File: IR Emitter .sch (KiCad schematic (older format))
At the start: 26 parts, among them U11 ULN2003APWR, U12 SMT_0540-S-R

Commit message: removed SD Card
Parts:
- R30, R31, R32, R33, R34, R35, R36: renamed from R?; footprint (none) -> Resistors_SMD:R_0603
- U11: footprint sop:TSSOP16 -> micromouse:ULN2003APWR
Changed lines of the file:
@@
 F 0 "U11" H 1850 4925 60  0000 L CNN
 F 1 "ULN2003APWR" H 1850 4825 60  0000 L CNN
-F 2 "sop:TSSOP16" H 1650 4675 60  0001 C CNN
+F 2 "micromouse:ULN2003APWR" H 1650 4675 60  0001 C CNN
 F 3 "" H 1650 4675 60  0001 C CNN
 	1    1650 4675
@@
 IR Emitter
 $Comp
-L R R?
+L R R30
 U 1 1 5976EE2D
 P 1300 4675
-F 0 "R?" V 1380 4675 50  0000 C CNN
+F 0 "R30" V 1380 4675 50  0000 C CNN
 F 1 "0" V 1300 4675 50  0000 C CNN
-F 2 "" V 1230 4675 50  0001 C CNN
+F 2 "Resistors_SMD:R_0603" V 1230 4675 50  0001 C CNN
 F 3 "" H 1300 4675 50  0001 C CNN
 	1    1300 4675
@@
 $EndComp
 $Comp
-L R R?
+L R R32
 U 1 1 5976F354
 P 1300 4875
-F 0 "R?" V 1380 4875 50  0000 C CNN
+F 0 "R32" V 1380 4875 50  0000 C CNN
 F 1 "0" V 1300 4875 50  0000 C CNN
-F 2 "" V 1230 4875 50  0001 C CNN
+F 2 "Resistors_SMD:R_0603" V 1230 4875 50  0001 C CNN
 F 3 "" H 1300 4875 50  0001 C CNN
 	1    1300 4875
@@
 $EndComp
 $Comp
-L R R?
+L R R31
 U 1 1 5976F3DE
 P 1300 4775
-F 0 "R?" V 1380 4775 50  0000 C CNN
+F 0 "R31" V 1380 4775 50  0000 C CNN
 F 1 "0" V 1300 4775 50  0000 C CNN
-F 2 "" V 1230 4775 50  0001 C CNN
+F 2 "Resistors_SMD:R_0603" V 1230 4775 50  0001 C CNN
 F 3 "" H 1300 4775 50  0001 C CNN
 	1    1300 4775
@@
 $EndComp
 $Comp
-L R R?
+L R R33
 U 1 1 5976F49C
 P 1300 4975
-F 0 "R?" V 1380 4975 50  0000 C CNN
+F 0 "R33" V 1380 4975 50  0000 C CNN
 F 1 "0" V 1300 4975 50  0000 C CNN
-F 2 "" V 1230 4975 50  0001 C CNN
+F 2 "Resistors_SMD:R_0603" V 1230 4975 50  0001 C CNN
 F 3 "" H 1300 4975 50  0001 C CNN
 	1    1300 4975
@@
 $EndComp
 $Comp
-L R R?
+L R R34
 U 1 1 5976F4F7
 P 1300 5075
-F 0 "R?" V 1380 5075 50  0000 C CNN
+F 0 "R34" V 1380 5075 50  0000 C CNN
 F 1 "0" V 1300 5075 50  0000 C CNN
-F 2 "" V 1230 5075 50  0001 C CNN
+F 2 "Resistors_SMD:R_0603" V 1230 5075 50  0001 C CNN
 F 3 "" H 1300 5075 50  0001 C CNN
 	1    1300 5075
@@
 $EndComp
 $Comp
-L R R?
+L R R35
 U 1 1 5976F557
 P 1300 5175
-F 0 "R?" V 1380 5175 50  0000 C CNN
+F 0 "R35" V 1380 5175 50  0000 C CNN
 F 1 "0" V 1300 5175 50  0000 C CNN
-F 2 "" V 1230 5175 50  0001 C CNN
+F 2 "Resistors_SMD:R_0603" V 1230 5175 50  0001 C CNN
 F 3 "" H 1300 5175 50  0001 C CNN
 	1    1300 5175
@@
 $EndComp
 $Comp
-L R R?
+L R R36
 U 1 1 5976F840
 P 1300 5275
-F 0 "R?" V 1380 5275 50  0000 C CNN
+F 0 "R36" V 1380 5275 50  0000 C CNN
 F 1 "0" V 1300 5275 50  0000 C CNN
-F 2 "" V 1230 5275 50  0001 C CNN
+F 2 "Resistors_SMD:R_0603" V 1230 5275 50  0001 C CNN
 F 3 "" H 1300 5275 50  0001 C CNN
 	1    1300 5275

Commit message: Added MPU-6500
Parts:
- removed R30, R31, R32, R33, R34, R35, R36: 0, Resistors_SMD:R_0603, symbol R
- added C30, C31: C, Capacitors_SMD:C_0603, symbol C
- D10, D12, D13, D8, D9: footprint LEDs:LED_D5.0mm_Horizontal_O3.81mm_Z3.0mm -> micromouse:IR-Emitter
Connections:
- wire segments 55 -> 53
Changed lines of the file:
@@
 EESchema Schematic File Version 2
+LIBS:device
+LIBS:Micromouse
 LIBS:power
-LIBS:device
 LIBS:transistors
 LIBS:conn
@@
 LIBS:contrib
 LIBS:valves
-LIBS:Micromouse
 LIBS:1_PJC-Sandbox
 LIBS:Micromouse1.2-cache
@@
 $Descr A4 11693 8268
 encoding utf-8
-Sheet 4 7
+Sheet 4 8
 Title ""
 Date ""
@@
 F 0 "D9" H 3495 3520 50  0000 L CNN
 F 1 "IRL81A" H 3435 3340 50  0000 C CNN
-F 2 "LEDs:LED_D5.0mm_Horizontal_O3.81mm_Z3.0mm" H 3475 3625 50  0001 C CNN
+F 2 "micromouse:IR-Emitter" H 3475 3625 50  0001 C CNN
 F 3 "" H 3425 3450 50  0000 C CNN
 	1    3475 3450
@@
 F 0 "D10" H 5020 3495 50  0000 L CNN
 F 1 "IRL81A" H 4960 3315 50  0000 C CNN
-F 2 "LEDs:LED_D5.0mm_Horizontal_O3.81mm_Z3.0mm" H 5000 3600 50  0001 C CNN
+F 2 "micromouse:IR-Emitter" H 5000 3600 50  0001 C CNN
 F 3 "" H 4950 3425 50  0000 C CNN
 	1    5000 3425
@@
 F 0 "D12" H 7220 3495 50  0000 L CNN
 F 1 "IRL81A" H 7160 3315 50  0000 C CNN
-F 2 "LEDs:LED_D5.0mm_Horizontal_O3.81mm_Z3.0mm" H 7200 3600 50  0001 C CNN
+F 2 "micromouse:IR-Emitter" H 7200 3600 50  0001 C CNN
 F 3 "" H 7150 3425 50  0000 C CNN
 	1    7200 3425
@@
 F 0 "D8" H 2995 3520 50  0000 L CNN
 F 1 "IRL81A" H 2935 3340 50  0000 C CNN
-F 2 "LEDs:LED_D5.0mm_Horizontal_O3.81mm_Z3.0mm" H 2975 3625 50  0001 C CNN
+F 2 "micromouse:IR-Emitter" H 2975 3625 50  0001 C CNN
 F 3 "" H 2925 3450 50  0000 C CNN
 	1    2975 3450
@@
 F 0 "D13" H 7720 3495 50  0000 L CNN
 F 1 "IRL81A" H 7660 3315 50  0000 C CNN
-F 2 "LEDs:LED_D5.0mm_Horizontal_O3.81mm_Z3.0mm" H 7700 3600 50  0001 C CNN
+F 2 "micromouse:IR-Emitter" H 7700 3600 50  0001 C CNN
 F 3 "" H 7650 3425 50  0000 C CNN
 	1    7700 3425
@@
 	2975 3350 2975 2925
 Wire Wire Line
-	2650 2925 7700 2925
+	2650 2925 8200 2925
 Wire Wire Line
 	7700 2925 7700 3325
@@
 Text Notes 3900 1400 0    394  ~ 79
 IR Emitter
-$Comp
-L R R30
-U 1 1 5976EE2D
-P 1300 4675
-F 0 "R30" V 1380 4675 50  0000 C CNN
-F 1 "0" V 1300 4675 50  0000 C CNN
-F 2 "Resistors_SMD:R_0603" V 1230 4675 50  0001 C CNN
-F 3 "" H 1300 4675 50  0001 C CNN
-	1    1300 4675
-	0    1    1    0
-$EndComp
-$Comp
-L R R32
-U 1 1 5976F354
-P 1300 4875
-F 0 "R32" V 1380 4875 50  0000 C CNN
-F 1 "0" V 1300 4875 50  0000 C CNN
-F 2 "Resistors_SMD:R_0603" V 1230 4875 50  0001 C CNN
-F 3 "" H 1300 4875 50  0001 C CNN
-	1    1300 4875
-	0    1    1    0
-$EndComp
-$Comp
-L R R31
-U 1 1 5976F3DE
-P 1300 4775
-F 0 "R31" V 1380 4775 50  0000 C CNN
-F 1 "0" V 1300 4775 50  0000 C CNN
-F 2 "Resistors_SMD:R_0603" V 1230 4775 50  0001 C CNN
-F 3 "" H 1300 4775 50  0001 C CNN
-	1    1300 4775
-	0    1    1    0
-$EndComp
-$Comp
-L R R33
-U 1 1 5976F49C
-P 1300 4975
-F 0 "R33" V 1380 4975 50  0000 C CNN
-F 1 "0" V 1300 4975 50  0000 C CNN
-F 2 "Resistors_SMD:R_0603" V 1230 4975 50  0001 C CNN
-F 3 "" H 1300 4975 50  0001 C CNN
-	1    1300 4975
-	0    1    1    0
-$EndComp
-$Comp
-L R R34
-U 1 1 5976F4F7
-P 1300 5075
-F 0 "R34" V 1380 5075 50  0000 C CNN
-F 1 "0" V 1300 5075 50  0000 C CNN
-F 2 "Resistors_SMD:R_0603" V 1230 5075 50  0001 C CNN
-F 3 "" H 1300 5075 50  0001 C CNN
-	1    1300 5075
-	0    1    1    0
-$EndComp
-$Comp
-L R R35
-U 1 1 5976F557
-P 1300 5175
-F 0 "R35" V 1380 5175 50  0000 C CNN
-F 1 "0" V 1300 5175 50  0000 C CNN
-F 2 "Resistors_SMD:R_0603" V 1230 5175 50  0001 C CNN
-F 3 "" H 1300 5175 50  0001 C CNN
-	1    1300 5175
-	0    1    1    0
-$EndComp
-$Comp
-L R R36
-U 1 1 5976F840
-P 1300 5275
-F 0 "R36" V 1380 5275 50  0000 C CNN
-F 1 "0" V 1300 5275 50  0000 C CNN
-F 2 "Resistors_SMD:R_0603" V 1230 5275 50  0001 C CNN
-F 3 "" H 1300 5275 50  0001 C CNN
-	1    1300 5275
-	0    1    1    0
-$EndComp
-Wire Wire Line
-	925  4675 1150 4675
-Wire Wire Line
-	1450 4675 1650 4675
-Wire Wire Line
-	1650 4775 1450 4775
-Wire Wire Line
-	1150 4775 925  4775
-Wire Wire Line
-	925  4875 1150 4875
-Wire Wire Line
-	1450 4875 1650 4875
-Wire Wire Line
-	1650 4975 1450 4975
-Wire Wire Line
-	1150 4975 925  4975
-Wire Wire Line
-	925  5075 1150 5075
-Wire Wire Line
-	1150 5175 925  5175
-Wire Wire Line
-	1150 5275 925  5275
-Wire Wire Line
-	1450 5275 1650 5275
-Wire Wire Line
-	1650 5175 1450 5175
-Wire Wire Line
-	1450 5075 1650 5075
+Wire Wire Line
+	925  4675 1650 4675
+Wire Wire Line
+	925  4775 1650 4775
+Wire Wire Line
+	925  4875 1650 4875
+Wire Wire Line
+	925  4975 1650 4975
+Wire Wire Line
+	925  5075 1650 5075
+Wire Wire Line
+	925  5175 1650 5175
+Wire Wire Line
+	925  5275 1650 5275
+$Comp
+L C C30
+U 1 1 5984FA65
+P 8000 3500
+F 0 "C30" H 8025 3600 50  0000 L CNN
+F 1 "C" H 8025 3400 50  0000 L CNN
+F 2 "Capacitors_SMD:C_0603" H 8038 3350 50  0001 C CNN
+F 3 "" H 8000 3500 50  0001 C CNN
+	1    8000 3500
+	1    0    0    -1
+$EndComp
+$Comp
+L C C31
+U 1 1 5984FA6B
+P 8400 3500
+F 0 "C31" H 8425 3600 50  0000 L CNN
+F 1 "C" H 8425 3400 50  0000 L CNN
+F 2 "Capacitors_SMD:C_0603" H 8438 3350 50  0001 C CNN
+F 3 "" H 8400 3500 50  0001 C CNN
+	1    8400 3500
+	1    0    0    -1
+$EndComp
+Wire Wire Line
+	8000 3350 8400 3350
+Wire Wire Line
+	8000 3650 8400 3650
+Connection ~ 8200 3650
+Wire Wire Line
+	8200 2925 8200 3350
+Connection ~ 8200 3350
+Connection ~ 7700 2925
+Wire Wire Line
+	8200 3654 8200 3950
+Wire Wire Line
+	8200 3950 8198 3950
+Connection ~ 8198 3950
 $EndSCHEMATC

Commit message: finished floor planning
-replaced the TC4427 and H brige by a single DRV8833 chip
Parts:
- removed D7: D, Diodes_SMD:D_0603, symbol D
- removed U12: SMT_0540-S-R, micromouse:Buzzer_SMT-0540-S-R, symbol SMT_0540-S-R
- D10, D11, D12, D13, D8, D9: footprint micromouse:IR-Emitter -> micromouse:IR_Emitter; manf# (none) -> SFH 4545
- R15, R16, R17, R18, R19, R20: footprint Resistors_SMD:R_0603 -> micromouse:C_0402
- U11: footprint micromouse:ULN2003APWR -> micromouse:ULN2003V12; manf# (none) -> ULN2003V12PWR
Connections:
- net labels added: V1.8
- net labels removed: V3.3
- wire segments 53 -> 49
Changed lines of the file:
@@
 EESchema Schematic File Version 2
+LIBS:1_PJC-Sandbox
+LIBS:Micromouse1.2-rescue
+LIBS:Micromouse1.2-cache
+LIBS:74xgxx
+LIBS:74xx
+LIBS:ac-dc
+LIBS:actel
+LIBS:adc-dac
+LIBS:allegro
+LIBS:Altera
+LIBS:analog_devices
+LIBS:analog_switches
+LIBS:atmel
+LIBS:audio
+LIBS:battery_management
+LIBS:bbd
+LIBS:bosch
+LIBS:brooktre
+LIBS:cmos_ieee
+LIBS:cmos4000
+LIBS:conn
+LIBS:contrib
+LIBS:cypress
+LIBS:dc-dc
 LIBS:device
-LIBS:Micromouse
+LIBS:digital-audio
+LIBS:diode
+LIBS:display
+LIBS:dsp
+LIBS:elec-unifil
+LIBS:ESD_Protection
+LIBS:ftdi
+LIBS:gennum
+LIBS:graphic
+LIBS:hc11
+LIBS:intel
+LIBS:interface
+LIBS:ir
+LIBS:Lattice
+LIBS:leds
+LIBS:linear
+LIBS:logo
+LIBS:maxim
+LIBS:mechanical
+LIBS:memory
+LIBS:microchip
+LIBS:microchip_dspic33dsc
+LIBS:microchip_pic10mcu
+LIBS:microchip_pic12mcu
+LIBS:microchip_pic16mcu
+LIBS:microchip_pic18mcu
+LIBS:microchip_pic24mcu
+LIBS:microchip_pic32mcu
+LIBS:microcontrollers
+LIBS:modules
+LIBS:motor_drivers
+LIBS:motorola
+LIBS:motors
+LIBS:msp430
+LIBS:nordicsemi
+LIBS:nxp
+LIBS:nxp_armmcu
+LIBS:onsemi
+LIBS:opto
+LIBS:Oscillators
+LIBS:philips
 LIBS:power
+LIBS:Power_Management
+LIBS:powerint
+LIBS:pspice
+LIBS:references
+LIBS:regul
+LIBS:relays
+LIBS:rfcom
+LIBS:sensors
+LIBS:silabs
+LIBS:siliconi
+LIBS:stm8
+LIBS:stm32
+LIBS:supertex
+LIBS:switches
+LIBS:texas
+LIBS:transf
 LIBS:transistors
-LIBS:conn
-LIBS:linear
-LIBS:regul
-LIBS:74xx
-LIBS:cmos4000
-LIBS:adc-dac
-LIBS:memory
+LIBS:triac_thyristor
+LIBS:ttl_ieee
+LIBS:valves
+LIBS:video
+LIBS:wiznet
+LIBS:Worldsemi
+LIBS:Xicor
 LIBS:xilinx
-LIBS:microcontrollers
-LIBS:dsp
-LIBS:microchip
-LIBS:analog_switches
-LIBS:motorola
-LIBS:texas
-LIBS:intel
-LIBS:audio
-LIBS:interface
-LIBS:digital-audio
-LIBS:philips
-LIBS:display
-LIBS:cypress
-LIBS:siliconi
-LIBS:opto
-LIBS:atmel
-LIBS:contrib
-LIBS:valves
-LIBS:1_PJC-Sandbox
-LIBS:Micromouse1.2-cache
+LIBS:zetex
+LIBS:Zilog
 EELAYER 25 0
 EELAYER END
@@
 F 0 "D9" H 3495 3520 50  0000 L CNN
 F 1 "IRL81A" H 3435 3340 50  0000 C CNN
-F 2 "micromouse:IR-Emitter" H 3475 3625 50  0001 C CNN
+F 2 "micromouse:IR_Emitter" H 3475 3625 50  0001 C CNN
 F 3 "" H 3425 3450 50  0000 C CNN
+F 4 "SFH 4545" H 3475 3450 60  0001 C CNN "manf#"
 	1    3475 3450
 	0    -1   -1   0
@@
 F 0 "D10" H 5020 3495 50  0000 L CNN
 F 1 "IRL81A" H 4960 3315 50  0000 C CNN
-F 2 "micromouse:IR-Emitter" H 5000 3600 50  0001 C CNN
+F 2 "micromouse:IR_Emitter" H 5000 3600 50  0001 C CNN
 F 3 "" H 4950 3425 50  0000 C CNN
+F 4 "SFH 4545" H 5000 3425 60  0001 C CNN "manf#"
 	1    5000 3425
 	0    -1   -1   0
@@
 F 0 "D11" H 5720 3495 50  0000 L CNN
 F 1 "IRL81A" H 5660 3315 50  0000 C CNN
-F 2 "micromouse:IR-Emitter" H 5700 3600 50  0001 C CNN
+F 2 "micromouse:IR_Emitter" H 5700 3600 50  0001 C CNN
 F 3 "" H 5650 3425 50  0000 C CNN
+F 4 "SFH 4545" H 5700 3425 60  0001 C CNN "manf#"
 	1    5700 3425
 	0    -1   -1   0
@@
 F 0 "D12" H 7220 3495 50  0000 L CNN
 F 1 "IRL81A" H 7160 3315 50  0000 C CNN
-F 2 "micromouse:IR-Emitter" H 7200 3600 50  0001 C CNN
+F 2 "micromouse:IR_Emitter" H 7200 3600 50  0001 C CNN
 F 3 "" H 7150 3425 50  0000 C CNN
+F 4 "SFH 4545" H 7200 3425 60  0001 C CNN "manf#"
 	1    7200 3425
 	0    -1   -1   0
@@
 F 0 "R15" V 2855 4775 50  0000 C CNN
 F 1 "0.75" V 2775 4775 50  0000 C CNN
-F 2 "Resistors_SMD:R_0603" V 2705 4775 50  0001 C CNN
+F 2 "micromouse:C_0402" V 2705 4775 50  0001 C CNN
 F 3 "" H 2775 4775 50  0001 C CNN
 	1    2775 4775
@@
 F 0 "R16" V 3080 4875 50  0000 C CNN
 F 1 "0.75" V 3000 4875 50  0000 C CNN
-F 2 "Resistors_SMD:R_0603" V 2930 4875 50  0001 C CNN
+F 2 "micromouse:C_0402" V 2930 4875 50  0001 C CNN
 F 3 "" H 3000 4875 50  0001 C CNN
 	1    3000 4875
@@
 F 0 "R17" V 4280 4975 50  0000 C CNN
 F 1 "0.75" V 4200 4975 50  0000 C CNN
-F 2 "Resistors_SMD:R_0603" V 4130 4975 50  0001 C CNN
+F 2 "micromouse:C_0402" V 4130 4975 50  0001 C CNN
 F 3 "" H 4200 4975 50  0001 C CNN
 	1    4200 4975
@@
 F 0 "R18" V 5405 5075 50  0000 C CNN
 F 1 "0.75" V 5325 5075 50  0000 C CNN
-F 2 "Resistors_SMD:R_0603" V 5255 5075 50  0001 C CNN
+F 2 "micromouse:C_0402" V 5255 5075 50  0001 C CNN
 F 3 "" H 5325 5075 50  0001 C CNN
 	1    5325 5075
@@
 F 0 "R19" V 6730 5175 50  0000 C CNN
 F 1 "0.75" V 6650 5175 50  0000 C CNN
-F 2 "Resistors_SMD:R_0603" V 6580 5175 50  0001 C CNN
+F 2 "micromouse:C_0402" V 6580 5175 50  0001 C CNN
 F 3 "" H 6650 5175 50  0001 C CNN
 	1    6650 5175
@@
 F 0 "R20" V 7530 5275 50  0000 C CNN
 F 1 "0.75" V 7450 5275 50  0000 C CNN
-F 2 "Resistors_SMD:R_0603" V 7380 5275 50  0001 C CNN
+F 2 "micromouse:C_0402" V 7380 5275 50  0001 C CNN
 F 3 "" H 7450 5275 50  0001 C CNN
 	1    7450 5275
@@
 F 0 "D8" H 2995 3520 50  0000 L CNN
 F 1 "IRL81A" H 2935 3340 50  0000 C CNN
-F 2 "micromouse:IR-Emitter" H 2975 3625 50  0001 C CNN
+F 2 "micromouse:IR_Emitter" H 2975 3625 50  0001 C CNN
 F 3 "" H 2925 3450 50  0000 C CNN
+F 4 "SFH 4545" H 2975 3450 60  0001 C CNN "manf#"
 	1    2975 3450
 	0    -1   -1   0
@@
 F 0 "D13" H 7720 3495 50  0000 L CNN
 F 1 "IRL81A" H 7660 3315 50  0000 C CNN
-F 2 "micromouse:IR-Emitter" H 7700 3600 50  0001 C CNN
+F 2 "micromouse:IR_Emitter" H 7700 3600 50  0001 C CNN
 F 3 "" H 7650 3425 50  0000 C CNN
+F 4 "SFH 4545" H 7700 3425 60  0001 C CNN "manf#"
 	1    7700 3425
 	0    -1   -1   0
@@
 F 0 "U11" H 1850 4925 60  0000 L CNN
 F 1 "ULN2003APWR" H 1850 4825 60  0000 L CNN
-F 2 "micromouse:ULN2003APWR" H 1650 4675 60  0001 C CNN
+F 2 "micromouse:ULN2003V12" H 1650 4675 60  0001 C CNN
 F 3 "" H 1650 4675 60  0001 C CNN
+F 4 "ULN2003V12PWR" H 1650 4675 60  0001 C CNN "manf#"
 	1    1650 4675
 	1    0    0    -1
 $EndComp
 $Comp
-L SMT_0540-S-R U12
-U 1 1 59461CC9
-P 2200 3600
-F 0 "U12" H 2200 3200 59  0000 C CNN
-F 1 "SMT_0540-S-R" H 2200 4100 59  0000 C CNN
-F 2 "micromouse:Buzzer_SMT-0540-S-R" H 2200 3600 59  0001 C CNN
-F 3 "" H 2200 3600 59  0001 C CNN
-	1    2200 3600
-	1    0    0    -1
-$EndComp
-Wire Wire Line
-	2500 3700 2650 3700
-Wire Wire Line
-	2650 3700 2650 4675
-$Comp
-L GNDD #PWR08
+L GNDD #PWR015
 U 1 1 5946214E
 P 8350 4250
-F 0 "#PWR08" H 8350 4000 50  0001 C CNN
+F 0 "#PWR015" H 8350 4000 50  0001 C CNN
 F 1 "GNDD" H 8350 4100 50  0000 C CNN
 F 2 "" H 8350 4250 50  0001 C CNN
@@
 Connection ~ 6500 3650
 Wire Wire Line
-	2975 3350 2975 2925
-Wire Wire Line
-	2650 2925 8200 2925
+	2975 2925 2975 3350
+Wire Wire Line
+	2975 2925 8200 2925
 Wire Wire Line
 	7700 2925 7700 3325
@@
 Connection ~ 6500 2925
 Connection ~ 6500 3350
-Wire Wire Line
-	2500 3400 2650 3400
-Wire Wire Line
-	2650 3400 2650 2925
 Connection ~ 2975 2925
-$Comp
-L D D7
-U 1 1 5946296D
-P 2650 3550
-F 0 "D7" H 2650 3650 50  0000 C CNN
-F 1 "D" H 2650 3450 50  0000 C CNN
-F 2 "Diodes_SMD:D_0603" H 2650 3550 50  0001 C CNN
-F 3 "" H 2650 3550 50  0001 C CNN
-	1    2650 3550
-	0    1    1    0
-$EndComp
 Text GLabel 5000 2400 1    59   Input ~ 12
-V3.3
+V1.8
 Text GLabel 925  4775 0    39   Input ~ 8
 L_EMITTER
@@
 LD_EMITTER
 $Comp
-L GNDA #PWR09
+L GNDA #PWR016
 U 1 1 59463543
 P 1525 5650
-F 0 "#PWR09" H 1525 5400 50  0001 C CNN
+F 0 "#PWR016" H 1525 5400 50  0001 C CNN
 F 1 "GNDA" H 1525 5500 50  0000 C CNN
 F 2 "" H 1525 5650 50  0001 C CNN

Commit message: Change of direction
- I am changing my MCU from mk66fx1m0vmd18 to mk20dx256vlh7 as the QFN  package pcb layout is too expensive to manufacture and the  144 LQFP is takes too much real estate
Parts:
- removed U11: ULN2003APWR, micromouse:ULN2003V12, symbol ULN2003APWR
- added Q1, Q2, Q3, Q4, Q5, Q6: Q_NMOS_DGS, micromouse:DMG1012UW, symbol Q_NMOS_DGS
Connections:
- net labels removed: BUZZER, GNDA
- wire segments 49 -> 25
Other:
- moved on the sheet: C30, C31, D13, D8, R15, R16, R17, R18, R19, R20

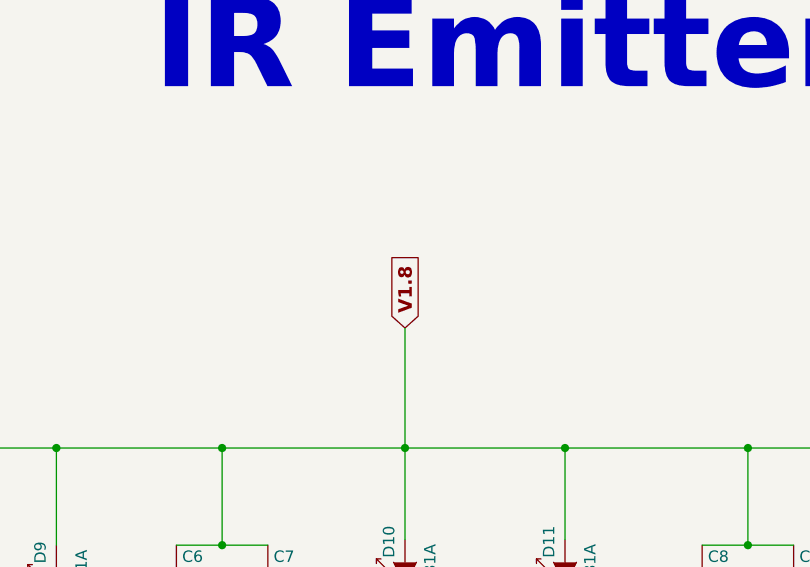
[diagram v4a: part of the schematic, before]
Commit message: added TPS61222DCK boost converter
-added TPS61222DCK boost converter for 5V input of the encoder
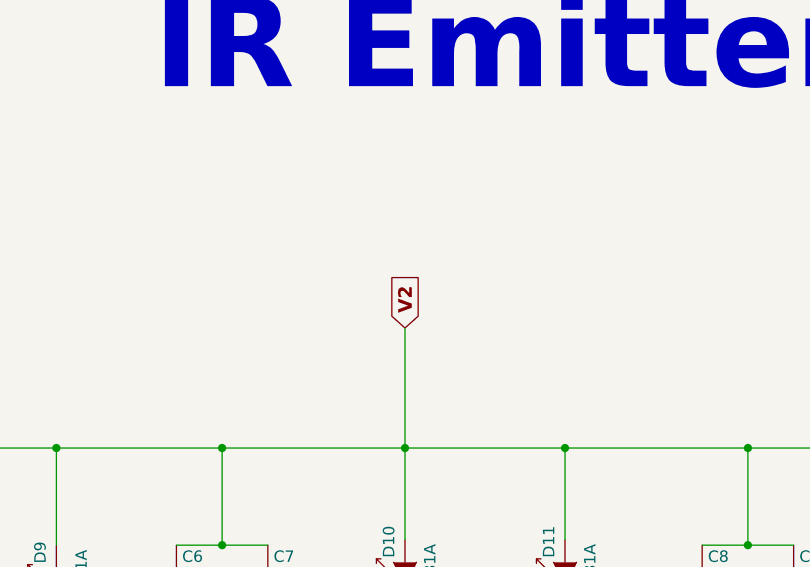
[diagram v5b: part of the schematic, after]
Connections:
- net V1.8 renamed V2
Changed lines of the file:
@@
 Connection ~ 6500 3350
 Text GLabel 5000 2400 1    59   Input ~ 12
-V1.8
+V2
 Text GLabel 2550 4425 0    39   Input ~ 8
 L_EMITTER

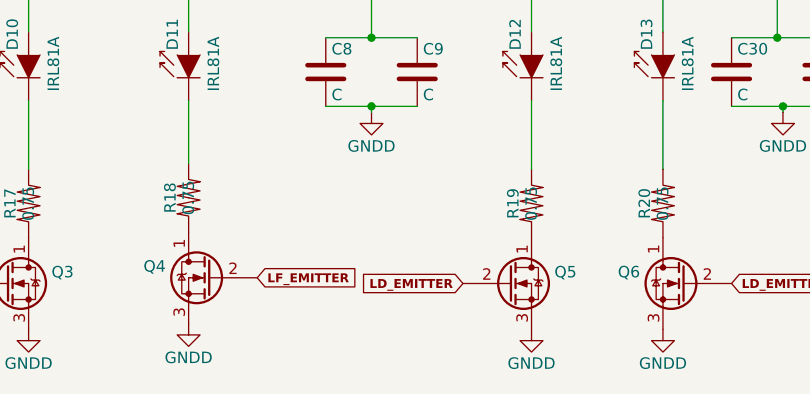
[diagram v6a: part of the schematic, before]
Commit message: wired up the MCU
-wired up the mcu to the gyro, motor controller.
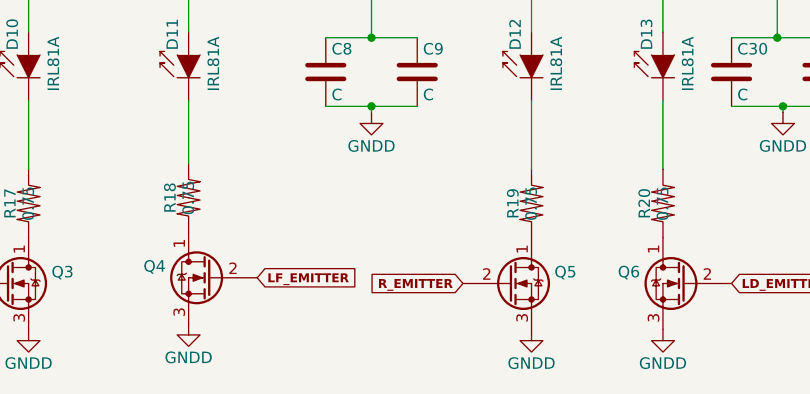
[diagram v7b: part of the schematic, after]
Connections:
- net LD_EMITTER: no longer Q5.2 (G)
- new net R_EMITTER: Q5.2 (G)
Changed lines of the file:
@@
 	6300 3650 6700 3650
 $Comp
-L GNDD #PWR17
+L GNDD #PWR014
 U 1 1 5946214E
 P 4200 3700
-F 0 "#PWR17" H 4200 3450 50  0001 C CNN
+F 0 "#PWR014" H 4200 3450 50  0001 C CNN
 F 1 "GNDD" H 4200 3550 50  0000 C CNN
 F 2 "" H 4200 3700 50  0001 C CNN
@@
 LF_EMITTER
 Text GLabel 6900 4425 0    39   Input ~ 8
-LD_EMITTER
+R_EMITTER
 Text GLabel 8075 4425 2    39   Input ~ 8
 LD_EMITTER
@@
 Connection ~ 4200 3650
 $Comp
-L GNDD #PWR20
+L GNDD #PWR015
 U 1 1 59D9D983
 P 6500 3675
-F 0 "#PWR20" H 6500 3425 50  0001 C CNN
+F 0 "#PWR015" H 6500 3425 50  0001 C CNN
 F 1 "GNDD" H 6500 3525 50  0000 C CNN
 F 2 "" H 6500 3675 50  0001 C CNN
@@
 $EndComp
 $Comp
-L GNDD #PWR23
+L GNDD #PWR016
 U 1 1 59D9DDA3
 P 8300 3675
-F 0 "#PWR23" H 8300 3425 50  0001 C CNN
+F 0 "#PWR016" H 8300 3425 50  0001 C CNN
 F 1 "GNDD" H 8300 3525 50  0000 C CNN
 F 2 "" H 8300 3675 50  0001 C CNN
@@
 $EndComp
 $Comp
-L GNDD #PWR22
+L GNDD #PWR017
 U 1 1 59DA4EAB
 P 7775 4625
-F 0 "#PWR22" H 7775 4375 50  0001 C CNN
+F 0 "#PWR017" H 7775 4375 50  0001 C CNN
 F 1 "GNDD" H 7775 4475 50  0000 C CNN
 F 2 "" H 7775 4625 50  0001 C CNN
@@
 $EndComp
 $Comp
-L GNDD #PWR21
+L GNDD #PWR018
 U 1 1 59DA52BE
 P 7200 4625
-F 0 "#PWR21" H 7200 4375 50  0001 C CNN
+F 0 "#PWR018" H 7200 4375 50  0001 C CNN
 F 1 "GNDD" H 7200 4475 50  0000 C CNN
 F 2 "" H 7200 4625 50  0001 C CNN
@@
 $EndComp
 $Comp
-L GNDD #PWR19
+L GNDD #PWR019
 U 1 1 59DA5311
 P 5700 4600
-F 0 "#PWR19" H 5700 4350 50  0001 C CNN
+F 0 "#PWR019" H 5700 4350 50  0001 C CNN
 F 1 "GNDD" H 5700 4450 50  0000 C CNN
 F 2 "" H 5700 4600 50  0001 C CNN
@@
 $EndComp
 $Comp
-L GNDD #PWR18
+L GNDD #PWR020
 U 1 1 59DA5544
 P 5000 4625
-F 0 "#PWR18" H 5000 4375 50  0001 C CNN
+F 0 "#PWR020" H 5000 4375 50  0001 C CNN
 F 1 "GNDD" H 5000 4475 50  0000 C CNN
 F 2 "" H 5000 4625 50  0001 C CNN
@@
 $EndComp
 $Comp
-L GNDD #PWR16
+L GNDD #PWR021
 U 1 1 59DA55E9
 P 3475 4625
-F 0 "#PWR16" H 3475 4375 50  0001 C CNN
+F 0 "#PWR021" H 3475 4375 50  0001 C CNN
 F 1 "GNDD" H 3475 4475 50  0000 C CNN
 F 2 "" H 3475 4625 50  0001 C CNN
@@
 $EndComp
 $Comp
-L GNDD #PWR15
+L GNDD #PWR022
 U 1 1 59DA587C
 P 2850 4625
-F 0 "#PWR15" H 2850 4375 50  0001 C CNN
+F 0 "#PWR022" H 2850 4375 50  0001 C CNN
 F 1 "GNDD" H 2850 4475 50  0000 C CNN
 F 2 "" H 2850 4625 50  0001 C CNN
